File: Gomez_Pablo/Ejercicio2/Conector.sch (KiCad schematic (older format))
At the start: 6 parts, among them U2 AMIS42665TJAA1RG

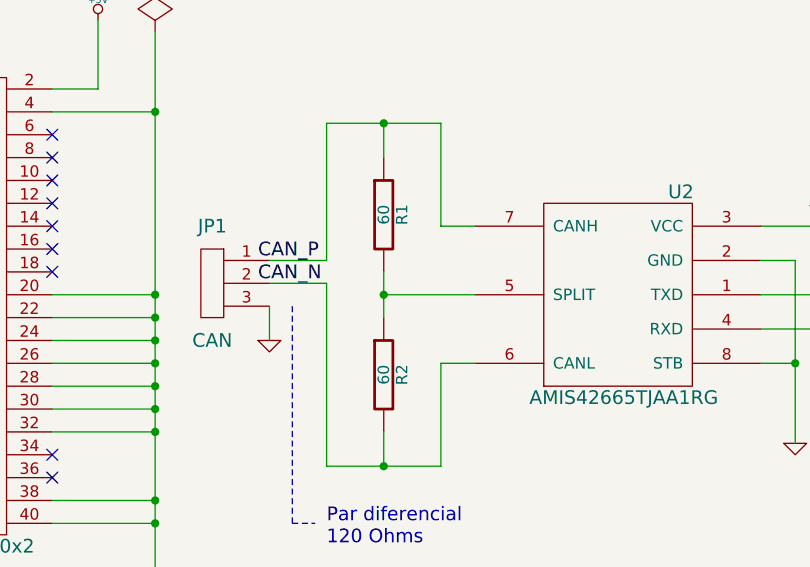
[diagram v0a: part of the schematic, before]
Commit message: se ecualizan pares diferenciales
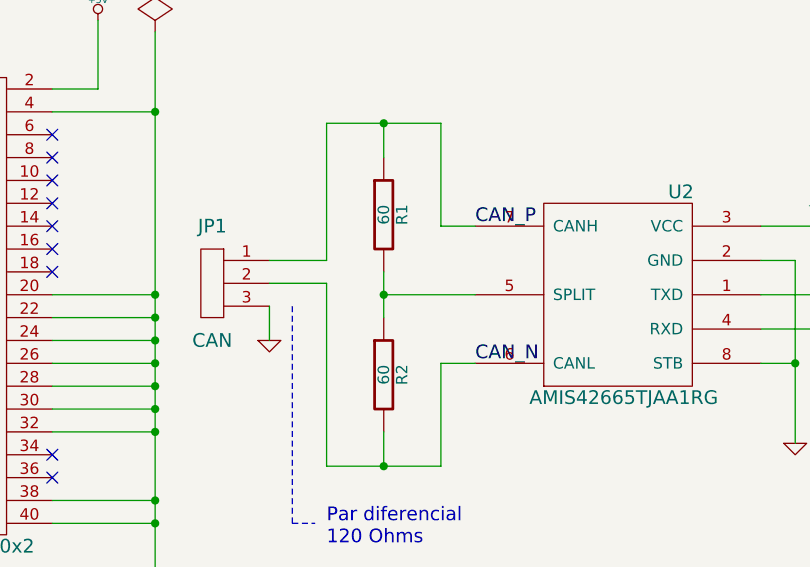
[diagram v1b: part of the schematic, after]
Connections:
- net CAN_N: now also JP1.2, R2.2, U2.6 (CANL)
- net CAN_P: now also JP1.1, R1.1, U2.7 (CANH)
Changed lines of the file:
@@
 EESchema Schematic File Version 2
 LIBS:ej2
+LIBS:Ejercicio2-cache
 EELAYER 25 0
 EELAYER END
@@
 Text Label 10100 3550 0    60   ~ 0
 CAN_RX
-Text Label 7650 3250 0    60   ~ 0
+Text Label 8600 3100 0    60   ~ 0
 CAN_P
-Text Label 7650 3350 0    60   ~ 0
+Text Label 8600 3700 0    60   ~ 0
 CAN_N
 Connection ~ 10100 3100
